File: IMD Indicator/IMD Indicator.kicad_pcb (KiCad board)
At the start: 2 copper layers, 42 x 31.5 mm, 14 parts, among them J5 776280-1, Q1 2N7002,215, Q2 2N7002,215

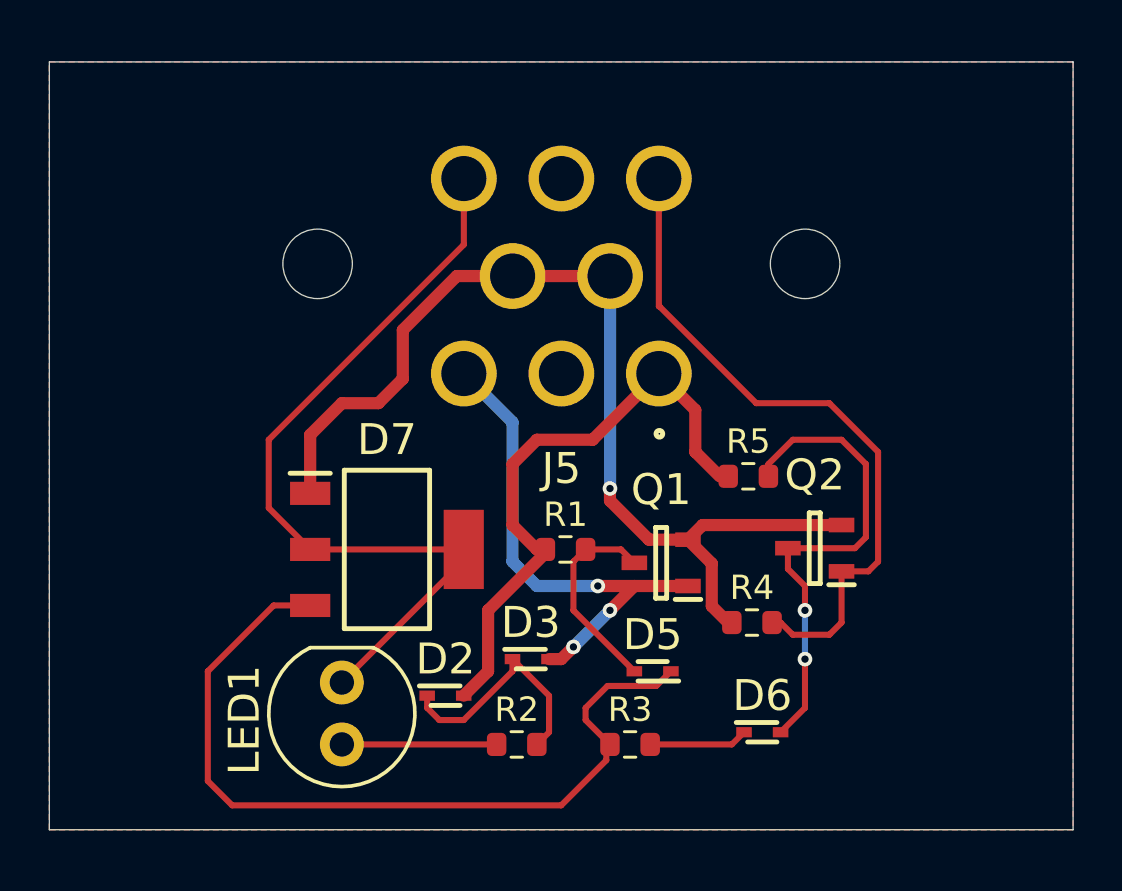
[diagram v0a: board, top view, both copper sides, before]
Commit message: shrank board outline, added 3D models
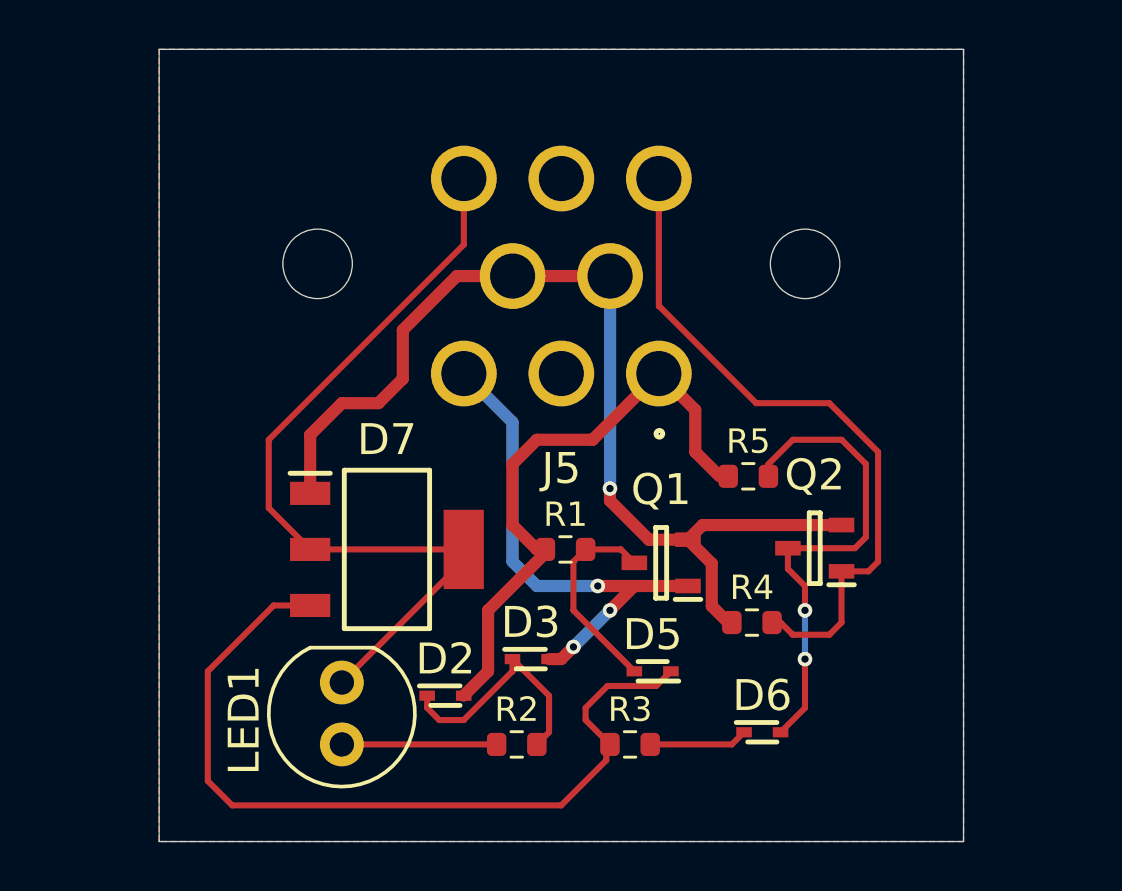
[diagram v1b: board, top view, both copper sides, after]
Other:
- board size 42 x 31.5 mm -> 33 x 32.5 mm
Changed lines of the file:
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@@
 		(capping no)
 		(filling no)
+		(grid_origin 166.005 58.48418)
 		(pcbplotparams
 			(layerselection 0x00000000_00000000_55555555_5755f5ff)
@@
 		)
 		(embedded_fonts no)
-		(model "HLMP-EG30-NR000.stp"
+		(model "C:/Users/mazha/Documents/SDM/IMD Indicator Project/HLMP-EG30-NR000/3D/HLMP-EG30-NR000.stp"
 			(offset
 				(xyz 0 0 0)
@@
 		)
 		(embedded_fonts no)
-		(model "${SDM_MISC_3D}/X0202MN_5BA4.step"
+		(model "C:/Users/mazha/Documents/SDM/IMD Indicator Project/X0202MN_5BA4/3D/X0202MN_5BA4.stp"
 			(offset
 				(xyz 0 0 1.849999996)
@@
 		)
 		(embedded_fonts no)
-		(model "${SDM_MISC_3D}/776280-1.step"
+		(model "C:/Users/mazha/Documents/SDM/IMD Indicator Project/776280-1/3D/776280-1.stp"
 			(offset
 				(xyz 0 -20 11.5)
@@
 		)
 	)
-	(gr_poly
-		(pts
-			(xy 145 59.5) (xy 187 59.5) (xy 187 91) (xy 145 91)
-		)
+	(gr_rect
+		(start 149.505 58.98418)
+		(end 182.505 91.48418)
 		(stroke
 			(width 0.05)
-			(type solid)
+			(type default)
 		)
 		(fill no)
@@
 		(polygon
 			(pts
-				(xy 145 59.5) (xy 187 59.5) (xy 187 91) (xy 145 91)
+				(xy 149.505 58.98418) (xy 182.505 58.98418) (xy 182.505 91.48418) (xy 149.505 91.48418)
 			)
 		)
@@
 		(polygon
 			(pts
-				(xy 145 59.5) (xy 187 59.5) (xy 187 91) (xy 145 91)
+				(xy 149.505 58.98418) (xy 182.505 58.98418) (xy 182.505 91.48418) (xy 149.505 91.48418)
 			)
 		)
